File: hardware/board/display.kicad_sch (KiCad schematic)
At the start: 15 parts, among them U32 SY7203DBC, U33 CY54-4.7UH

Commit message: finished schematic!
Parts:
- added C369, C370: 100nF X5R 10V, Capacitor_SMD:C_0201_0603Metric, symbol Device:C
- added U1: RK3568, RK3568:BGA636C65P28X28_1900X1900X168, symbol RK3568:RK3568
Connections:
- net GND: now also C369.2, C370.2
- net MIPI_DSI_TX0_CLKN: now also U1.AG15 (MIPI_DSI_TX0_CLKN/LVDS_TX0_CLKN)
- net MIPI_DSI_TX0_CLKP: now also U1.AH15 (MIPI_DSI_TX0_CLKP/LVDS_TX0_CLKP)
- net MIPI_DSI_TX0_D0N: now also U1.AG17 (MIPI_DSI_TX0_D0N/LVDS_TX0_D0N)
- net MIPI_DSI_TX0_D0P: now also U1.AH17 (MIPI_DSI_TX0_D0P/LVDS_TX0_D0P)
- net MIPI_DSI_TX0_D1N: now also U1.AG16 (MIPI_DSI_TX0_D1N/LVDS_TX0_D1N)
- net MIPI_DSI_TX0_D1P: now also U1.AH16 (MIPI_DSI_TX0_D1P/LVDS_TX0_D1P)
- net MIPI_DSI_TX0_D2N: now also U1.AG14 (MIPI_DSI_TX0_D2N/LVDS_TX0_D2N)
- net MIPI_DSI_TX0_D2P: now also U1.AH14 (MIPI_DSI_TX0_D2P/LVDS_TX0_D2P)
- net MIPI_DSI_TX0_D3N: now also U1.AG13 (MIPI_DSI_TX0_D3N/LVDS_TX0_D3N)
- net MIPI_DSI_TX0_D3P: now also U1.AH13 (MIPI_DSI_TX0_D3P/LVDS_TX0_D3P)
- net LCD_RST_L_GPIO3_C7 renamed LCD_RST_L_GPIO2_D6
- new net MIPI_AVDD_0V9: C370.1, U1.W16 (MIPI_DSI_TX0/LVDS_TX0_AVDD_0V9)
- new net MIPI_AVDD_1V8: C369.1, U1.Y17 (MIPI_DSI_TX0/LVDS_TX0_AVDD_1V8)
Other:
- note added: "Diff 100 Ohm ±10%"
- note added: "Display"

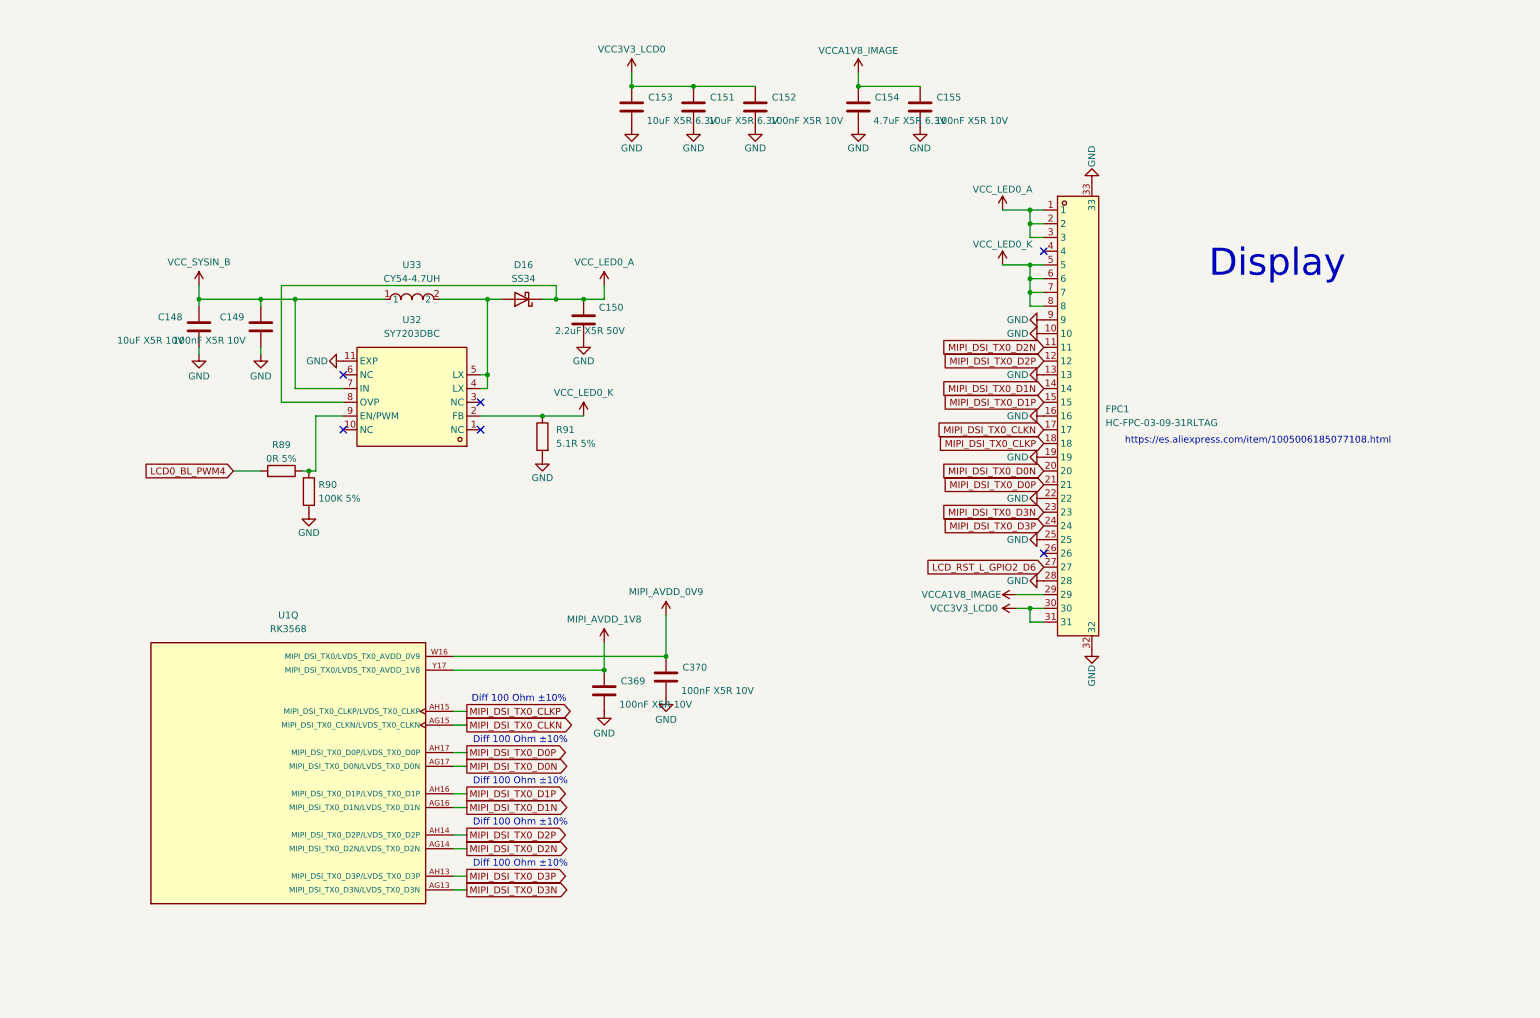
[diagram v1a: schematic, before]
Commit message: finished beautifying schematic
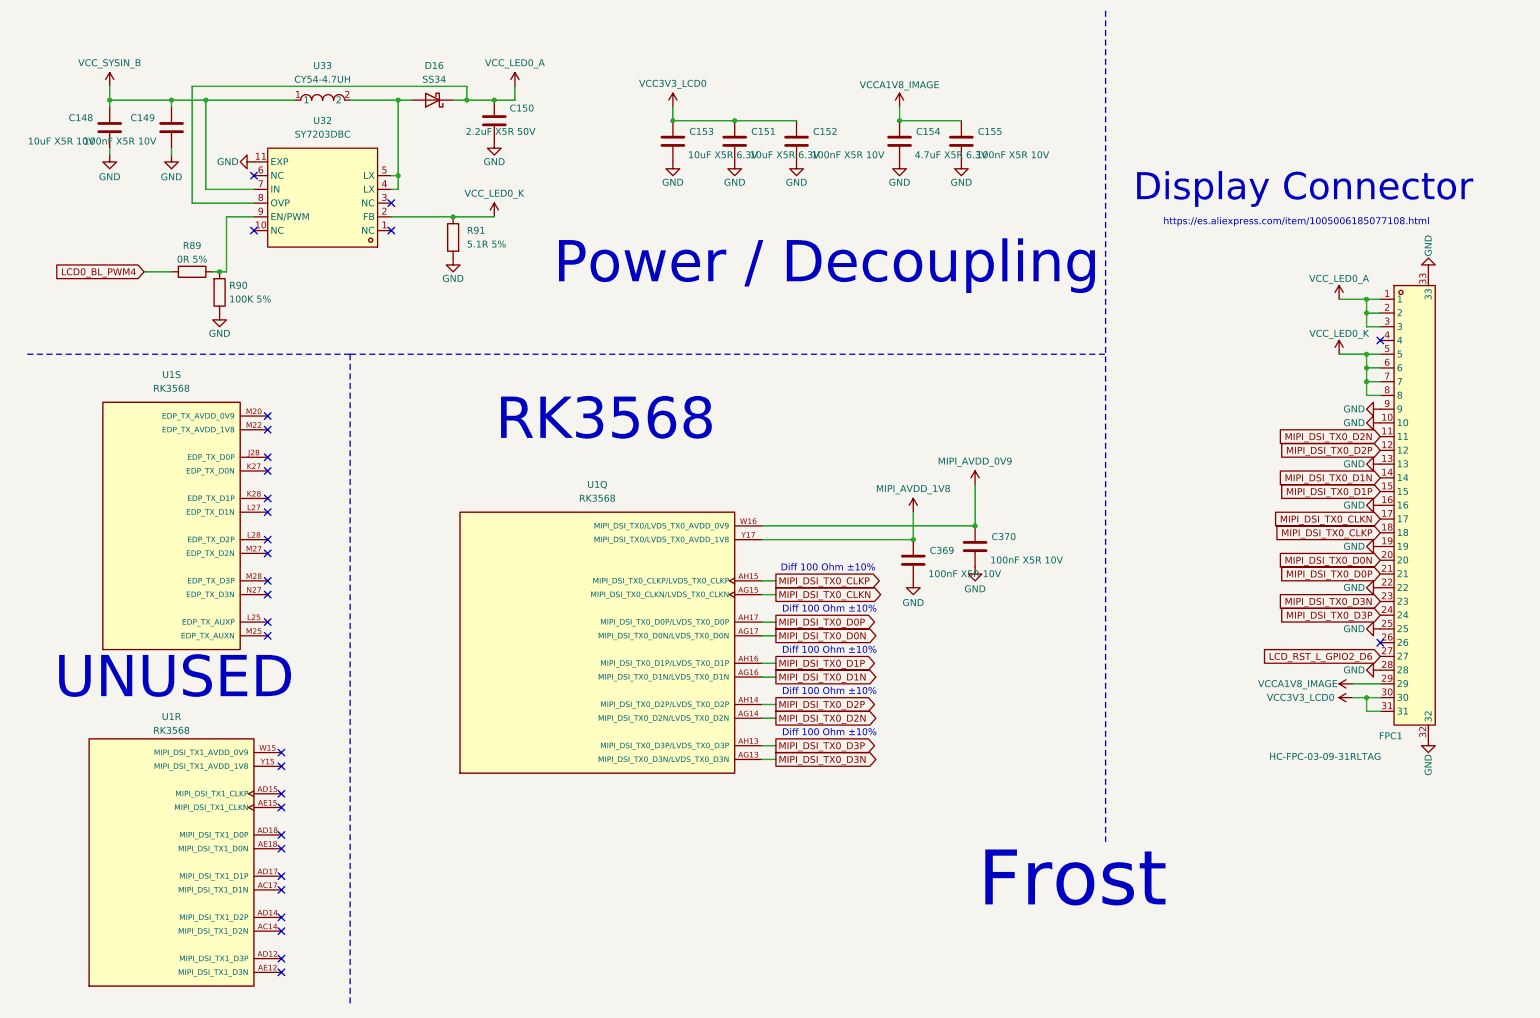
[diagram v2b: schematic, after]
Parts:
- added unit 18 of U1
- added unit 19 of U1
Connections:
- no-connect marks 6 -> 30
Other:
- note added: "Display Connector"
- note added: "Frost"
- note added: "Power / Decoupling"
- note added: "RK3568"
- note added: "UNUSED"
- note removed: "Display"
- moved on the sheet: C148, C149, C150, C151, C152, C153, C154, C155, C369, C370, D16, FPC1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
